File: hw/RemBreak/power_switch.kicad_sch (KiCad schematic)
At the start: 39 parts, among them Q11 BC337, Q12 BC847, Q3 BC847, Q6 BC337, Q7 BC847, Q8 SiS415DNT, Q9 BC337, U1 L7805, U2 L7805, U3 XC6220B331MR, U4 MAX40200AUK, U8 BD48ExxG, U9 BD48ExxG

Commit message: finished schematics routing and erc passed
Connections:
- net 3V3 renamed +3V3
- net 5V renamed +5V
- net 7V4 renamed +7.5V
- net RUNNIG renamed RUNNIG (RED)
- net SW+ renamed VBATT
- net SW- renamed ON/OFF
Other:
- moved on the sheet: R23, R24

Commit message: regenerated anotations and used battery connector with grounding
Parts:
- renumbered C1 to C2, C2 to C3, C3 to C4, Q7 to Q3, Q6 to Q4, Q11 to Q5, Q8 to Q6, Q12 to Q7, Q9 to Q8, Q3 to Q9, R23 to R14, R24 to R15, R32 to R16, R31 to R17, R25 to R18, R33 to R19, R36 to R20, R37 to R21, R26 to R22, R35 to R23, R28 to R24, R29 to R25, R27 to R26, R40 to R27, R34 to R28, R38 to R29, R39 to R30, R30 to R31, R43 to R32, R44 to R33, R10 to R34, R42 to R35, R41 to R36, U8 to U3, U9 to U4, U1 to U5, U2 to U6, U3 to U7, U4 to U8

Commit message: changed board settings and replaced r and c footprints with the ones for handsoldering
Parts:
- C2, C3, C4: footprint Capacitor_SMD:C_0805_2012Metric -> Capacitor_SMD:C_0805_2012Metric_Pad1.18x1.45mm_HandSolder
- R14, R15, R16, R17, R18, R19, R20, R21, R22, R23, R24, R25, R26, R27, R28, R29, R30, R31, R32, R33, R34, R35, R36: footprint Resistor_SMD:R_0805_2012Metric -> Resistor_SMD:R_0805_2012Metric_Pad1.20x1.40mm_HandSolder
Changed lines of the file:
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@@
 			)
 		)
-		(property "Footprint" "Resistor_SMD:R_0805_2012Metric"
+		(property "Footprint" "Resistor_SMD:R_0805_2012Metric_Pad1.20x1.40mm_HandSolder"
 			(at 36.068 88.9 90)
 			(effects
@@
 			)
 		)
-		(property "Footprint" "Resistor_SMD:R_0805_2012Metric"
+		(property "Footprint" "Resistor_SMD:R_0805_2012Metric_Pad1.20x1.40mm_HandSolder"
 			(at 122.428 111.76 90)
 			(effects
@@
 			)
 		)
-		(property "Footprint" "Resistor_SMD:R_0805_2012Metric"
+		(property "Footprint" "Resistor_SMD:R_0805_2012Metric_Pad1.20x1.40mm_HandSolder"
 			(at 191.77 112.268 90)
 			(effects
@@
 			)
 		)
-		(property "Footprint" "Resistor_SMD:R_0805_2012Metric"
+		(property "Footprint" "Resistor_SMD:R_0805_2012Metric_Pad1.20x1.40mm_HandSolder"
 			(at 58.42 168.402 90)
 			(effects
@@
 			)
 		)
-		(property "Footprint" "Capacitor_SMD:C_0805_2012Metric"
+		(property "Footprint" "Capacitor_SMD:C_0805_2012Metric_Pad1.18x1.45mm_HandSolder"
 			(at 238.4552 72.39 0)
 			(effects
@@
 			)
 		)
-		(property "Footprint" "Resistor_SMD:R_0805_2012Metric"
+		(property "Footprint" "Resistor_SMD:R_0805_2012Metric_Pad1.20x1.40mm_HandSolder"
 			(at 80.772 130.81 90)
 			(effects
@@
 			)
 		)
-		(property "Footprint" "Resistor_SMD:R_0805_2012Metric"
+		(property "Footprint" "Resistor_SMD:R_0805_2012Metric_Pad1.20x1.40mm_HandSolder"
 			(at 95.25 51.308 90)
 			(effects
@@
 			)
 		)
-		(property "Footprint" "Resistor_SMD:R_0805_2012Metric"
+		(property "Footprint" "Resistor_SMD:R_0805_2012Metric_Pad1.20x1.40mm_HandSolder"
 			(at 218.948 129.54 90)
 			(effects
@@
 			)
 		)
-		(property "Footprint" "Resistor_SMD:R_0805_2012Metric"
+		(property "Footprint" "Resistor_SMD:R_0805_2012Metric_Pad1.20x1.40mm_HandSolder"
 			(at 109.982 130.81 90)
 			(effects
@@
 			)
 		)
-		(property "Footprint" "Resistor_SMD:R_0805_2012Metric"
+		(property "Footprint" "Resistor_SMD:R_0805_2012Metric_Pad1.20x1.40mm_HandSolder"
 			(at 69.342 180.34 90)
 			(effects
@@
 			)
 		)
-		(property "Footprint" "Capacitor_SMD:C_0805_2012Metric"
+		(property "Footprint" "Capacitor_SMD:C_0805_2012Metric_Pad1.18x1.45mm_HandSolder"
 			(at 186.3852 60.96 0)
 			(effects
@@
 			)
 		)
-		(property "Footprint" "Resistor_SMD:R_0805_2012Metric"
+		(property "Footprint" "Resistor_SMD:R_0805_2012Metric_Pad1.20x1.40mm_HandSolder"
 			(at 93.98 83.058 90)
 			(effects
@@
 			)
 		)
-		(property "Footprint" "Resistor_SMD:R_0805_2012Metric"
+		(property "Footprint" "Resistor_SMD:R_0805_2012Metric_Pad1.20x1.40mm_HandSolder"
 			(at 223.52 120.142 90)
 			(effects
@@
 			)
 		)
-		(property "Footprint" "Resistor_SMD:R_0805_2012Metric"
+		(property "Footprint" "Resistor_SMD:R_0805_2012Metric_Pad1.20x1.40mm_HandSolder"
 			(at 110.998 58.42 90)
 			(effects
@@
 			)
 		)
-		(property "Footprint" "Resistor_SMD:R_0805_2012Metric"
+		(property "Footprint" "Resistor_SMD:R_0805_2012Metric_Pad1.20x1.40mm_HandSolder"
 			(at 133.35 98.552 90)
 			(effects
@@
 			)
 		)
-		(property "Footprint" "Resistor_SMD:R_0805_2012Metric"
+		(property "Footprint" "Resistor_SMD:R_0805_2012Metric_Pad1.20x1.40mm_HandSolder"
 			(at 84.328 74.93 90)
 			(effects
@@
 			)
 		)
-		(property "Footprint" "Resistor_SMD:R_0805_2012Metric"
+		(property "Footprint" "Resistor_SMD:R_0805_2012Metric_Pad1.20x1.40mm_HandSolder"
 			(at 97.79 152.908 90)
 			(effects
@@
 			)
 		)
-		(property "Footprint" "Resistor_SMD:R_0805_2012Metric"
+		(property "Footprint" "Resistor_SMD:R_0805_2012Metric_Pad1.20x1.40mm_HandSolder"
 			(at 36.068 118.11 90)
 			(effects
@@
 			)
 		)
-		(property "Footprint" "Resistor_SMD:R_0805_2012Metric"
+		(property "Footprint" "Resistor_SMD:R_0805_2012Metric_Pad1.20x1.40mm_HandSolder"
 			(at 185.928 100.33 90)
 			(effects
@@
 			)
 		)
-		(property "Footprint" "Resistor_SMD:R_0805_2012Metric"
+		(property "Footprint" "Resistor_SMD:R_0805_2012Metric_Pad1.20x1.40mm_HandSolder"
 			(at 97.79 171.958 90)
 			(effects
@@
 			)
 		)
-		(property "Footprint" "Resistor_SMD:R_0805_2012Metric"
+		(property "Footprint" "Resistor_SMD:R_0805_2012Metric_Pad1.20x1.40mm_HandSolder"
 			(at 119.38 163.068 90)
 			(effects
@@
 			)
 		)
-		(property "Footprint" "Capacitor_SMD:C_0805_2012Metric"
+		(property "Footprint" "Capacitor_SMD:C_0805_2012Metric_Pad1.18x1.45mm_HandSolder"
 			(at 157.1752 60.96 0)
 			(effects
@@
 			)
 		)
-		(property "Footprint" "Resistor_SMD:R_0805_2012Metric"
+		(property "Footprint" "Resistor_SMD:R_0805_2012Metric_Pad1.20x1.40mm_HandSolder"
 			(at 201.168 68.58 90)
 			(effects
@@
 			)
 		)
-		(property "Footprint" "Resistor_SMD:R_0805_2012Metric"
+		(property "Footprint" "Resistor_SMD:R_0805_2012Metric_Pad1.20x1.40mm_HandSolder"
 			(at 93.98 102.108 90)
 			(effects
@@
 			)
 		)
-		(property "Footprint" "Resistor_SMD:R_0805_2012Metric"
+		(property "Footprint" "Resistor_SMD:R_0805_2012Metric_Pad1.20x1.40mm_HandSolder"
 			(at 97.79 142.748 90)
 			(effects
@@
 			)
 		)
-		(property "Footprint" "Resistor_SMD:R_0805_2012Metric"
+		(property "Footprint" "Resistor_SMD:R_0805_2012Metric_Pad1.20x1.40mm_HandSolder"
 			(at 191.77 123.698 90)
 			(effects

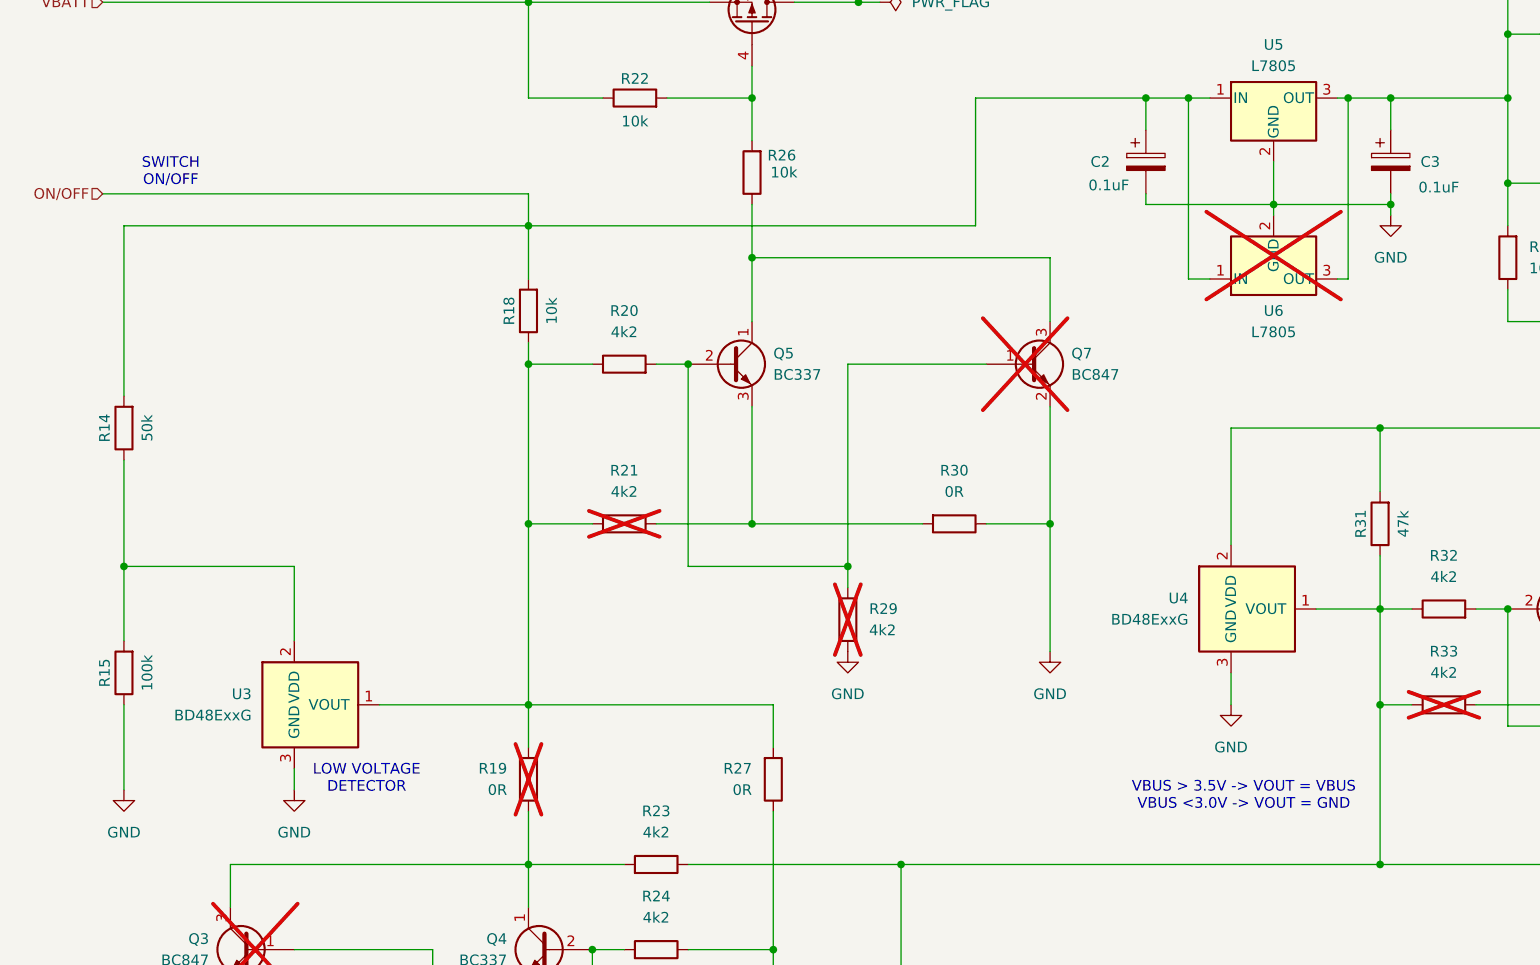
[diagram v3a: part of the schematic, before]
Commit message: Note fonts changed to bold and added titles of the sheets included rev number
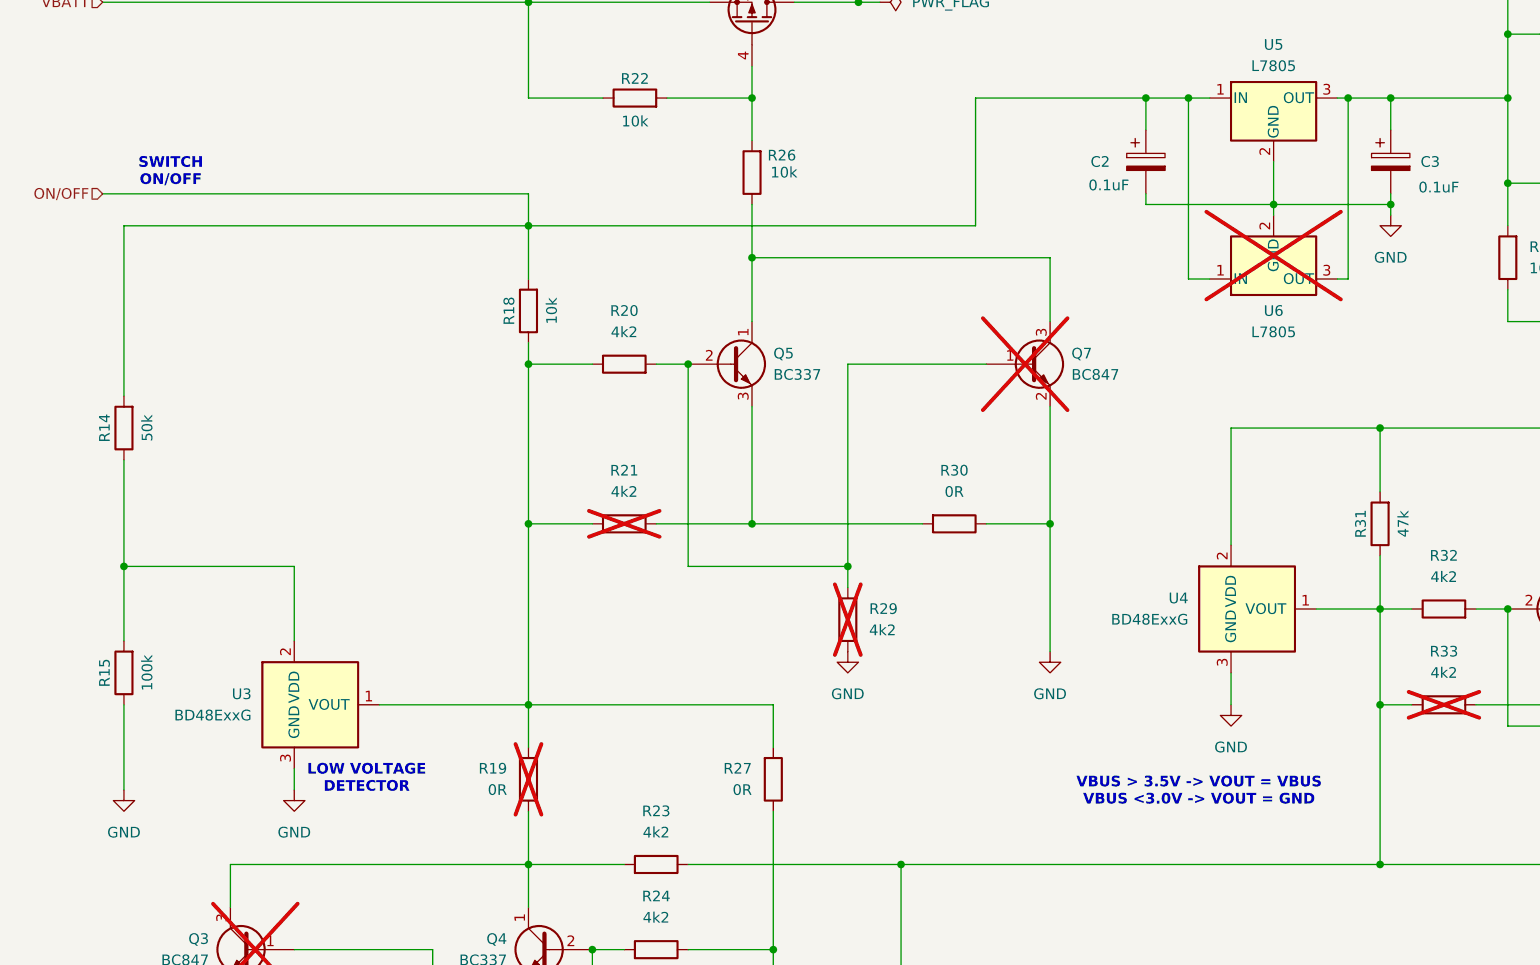
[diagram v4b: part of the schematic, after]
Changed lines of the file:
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@@
 	(title_block
 		(title "Power Control")
+		(date "2024-12-15")
+		(rev "1.0")
 	)
 	(text "VBUS > 3.5V -> VOUT = VBUS\nVBUS <3.0V -> VOUT = GND"
 		(exclude_from_sim no)
-		(at 167.894 132.842 0)
+		(at 162.56 132.334 0)
 		(effects
 			(font
 				(size 1.27 1.27)
+				(thickness 0.254)
+				(bold yes)
 			)
 		)
@@
 			(font
 				(size 1.27 1.27)
+				(thickness 0.254)
+				(bold yes)
 			)
 		)
@@
 			(font
 				(size 1.27 1.27)
+				(thickness 0.254)
+				(bold yes)
 			)
 		)
